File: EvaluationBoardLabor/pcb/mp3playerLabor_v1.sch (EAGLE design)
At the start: 25 parts, among them IC1 4050N, Q1 12MHz, X1 FPS009-3000, X2 1503_09

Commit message: update schematic
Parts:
- added LED1, LED2, LED3: (no value), led:LEDSML1206
- added R10, R11, R12: 390, rcl:R-EU_R1206
- added R2, R8, R9: 100k, rcl:R-EU_R1206
- added SV5: (no value), con-lstb:MA04-1
- R1, R3, R4, R5, R6, R7: device rcl:R-EU_M1206 -> rcl:R-EU_R1206
- X1: value FPS009-3000 -> SD-Card holder
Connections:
- removed net AREF: SV3.3
- removed net N$1: U$1.P$12, X1.5
- removed net N$15: U$1.P$1
- removed net N$17: R7.1, U$1.P$26
- removed net N$2: U$1.P$14, X1.7
- removed net N$3: U$1.P$13, X1.2
- new net CSCARD: IC1C.O, X1.1
- new net MOSI: IC1B.O, U$1.P$13, X1.2
- new net SCK: IC1A.O, U$1.P$12, X1.5
- new net XCS: IC1D.O, U$1.P$11
- new net XDCS: IC1E.O, U$1.P$4
- new net XRESET: IC1F.O, R7.1, U$1.P$26
- net +3V3: now also C5.1, IC1P.VDD, SV3.3
- net +5V: now also S1.S, S2.S, S3.S, SV5.2
- net GND: now also C5.2, R10.2, R11.2, R12.2, R2.2, R8.2, R9.2, SV5.1
- net N$4: now also LED1.C, R10.1; no longer U$1.P$11
- net N$5: now also LED2.C, R11.1; no longer X1.1
- net N$7: now also LED3.C, R12.1; no longer U$1.P$4
- net PB1: now also IC1C.I
- net PB2: now also IC1D.I
- net PB3: now also IC1B.I
- net PB4: now also U$1.P$14, X1.7
- net PB5: now also IC1A.I
- net PC0: now also IC1E.I
- net PC1: now also U$1.P$1
- net PC3: now also IC1F.I
- net PC4: now also SV5.4
- net PC5: now also SV5.3
- net PD2: now also R2.1, S1.P
- net PD3: now also R8.1, S2.P
- net PD4: now also R9.1, S3.P
- net PD5: now also LED1.A
- net PD6: now also LED2.A
- net PD7: now also LED3.A
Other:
- note added: "(DREQ)"
- note added: "(MISO)"
- note added: "(SCL)"
- note added: "(SDA)"
- note added: "ATmega328-XPlained"
- note added: "I2C Display"
- note added: "Level Shifter (5V->3,3V)"
- note added: "MP3-Decoder"
- note added: "PB0 = PB1 = CS Card PB2 = XCS (MP3-Decoder) PB3 = MOSI (SPI) PB4 = MISO (SPI) PB5 = SCK (SPI)"
- note added: "PC0 = XDCS (MP3-Decoder) PC1 = DREQ (MP3-Decoder) PC2 = PC3 = XRESET (MP3-Decoder) PC4 = SDA ( I2C Display ) PC5 = SCL ( I2C Display )"
- note added: "PD0 = RX PD1 = TX PD2 = S1 Taster PD3 = S2 Taster PD4 = S3 Taster PD5 = LED1 PD6 = LED2 PD7 = LED3"
- moved on the sheet: C5, IC1A, IC1B, IC1C, IC1D, IC1E, IC1F, IC1P, S1, S2, S3

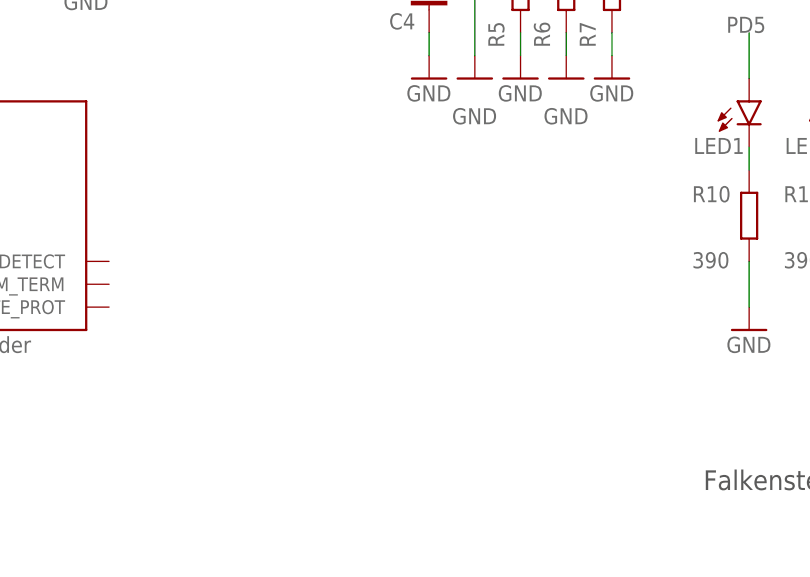
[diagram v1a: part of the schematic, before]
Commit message: DisplayTest added
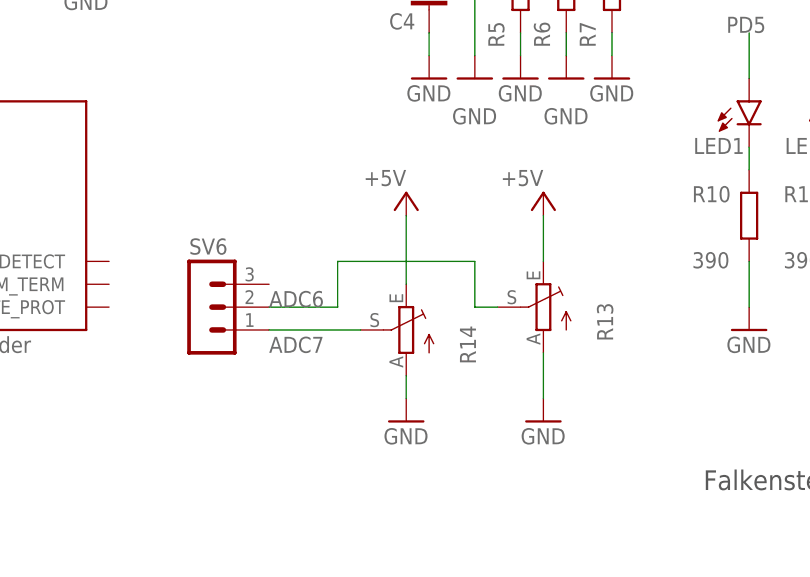
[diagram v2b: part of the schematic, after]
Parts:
- added R13, R14: (no value), pot:TRIM_EU-CA6V
- added SV6: (no value), con-lstb:MA03-1
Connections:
- new net ADC6: R13.S, SV6.2
- new net ADC7: R14.S, SV6.1
- net +5V: now also R13.E, R14.E
- net GND: now also R13.A, R14.A
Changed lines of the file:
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@@
 <part name="GND21" library="supply1" deviceset="GND" device=""/>
 <part name="GND22" library="supply1" deviceset="GND" device=""/>
+<part name="SV6" library="con-lstb" library_urn="urn:adsk.eagle:library:162" deviceset="MA03-1" device="" package3d_urn="urn:adsk.eagle:package:8339/1"/>
+<part name="R13" library="pot" library_urn="urn:adsk.eagle:library:331" deviceset="TRIM_EU-" device="CA6V" package3d_urn="urn:adsk.eagle:package:22691/1"/>
+<part name="R14" library="pot" library_urn="urn:adsk.eagle:library:331" deviceset="TRIM_EU-" device="CA6V" package3d_urn="urn:adsk.eagle:package:22691/1"/>
+<part name="GND15" library="supply1" deviceset="GND" device=""/>
+<part name="GND23" library="supply1" deviceset="GND" device=""/>
+<part name="P+6" library="supply1" library_urn="urn:adsk.eagle:library:371" deviceset="+5V" device=""/>
+<part name="P+7" library="supply1" library_urn="urn:adsk.eagle:library:371" deviceset="+5V" device=""/>
 </parts>
 <sheets>
@@
 <attribute name="VALUE" x="241.3" y="35.56" size="1.778" layer="96"/>
 </instance>
+<instance part="SV6" gate="G$1" x="162.56" y="40.64" smashed="yes">
+<attribute name="VALUE" x="161.29" y="33.02" size="1.778" layer="96"/>
+<attribute name="NAME" x="161.29" y="46.482" size="1.778" layer="95"/>
+</instance>
+<instance part="R13" gate="1" x="200.66" y="40.64" smashed="yes" rot="MR0">
+<attribute name="NAME" x="206.629" y="36.83" size="1.778" layer="95" rot="MR90"/>
+<attribute name="VALUE" x="204.47" y="36.83" size="1.778" layer="96" rot="MR90"/>
+</instance>
+<instance part="R14" gate="1" x="185.42" y="38.1" smashed="yes" rot="MR0">
+<attribute name="NAME" x="191.389" y="34.29" size="1.778" layer="95" rot="MR90"/>
+<attribute name="VALUE" x="189.23" y="34.29" size="1.778" layer="96" rot="MR90"/>
+</instance>
+<instance part="GND15" gate="1" x="200.66" y="27.94" smashed="yes">
+<attribute name="VALUE" x="198.12" y="25.4" size="1.778" layer="96"/>
+</instance>
+<instance part="GND23" gate="1" x="185.42" y="27.94" smashed="yes">
+<attribute name="VALUE" x="182.88" y="25.4" size="1.778" layer="96"/>
+</instance>
+<instance part="P+6" gate="1" x="200.66" y="53.34" smashed="yes">
+<attribute name="VALUE" x="200.66" y="55.88" size="1.778" layer="96" rot="R180"/>
+</instance>
+<instance part="P+7" gate="1" x="185.42" y="53.34" smashed="yes">
+<attribute name="VALUE" x="185.42" y="55.88" size="1.778" layer="96" rot="R180"/>
+</instance>
 </instances>
 <busses>
@@
 <wire x1="243.84" y1="45.72" x2="243.84" y2="40.64" width="0.1524" layer="91"/>
 </segment>
+<segment>
+<pinref part="R14" gate="1" pin="A"/>
+<pinref part="GND23" gate="1" pin="GND"/>
+<wire x1="185.42" y1="33.02" x2="185.42" y2="30.48" width="0.1524" layer="91"/>
+</segment>
+<segment>
+<pinref part="R13" gate="1" pin="A"/>
+<pinref part="GND15" gate="1" pin="GND"/>
+<wire x1="200.66" y1="35.56" x2="200.66" y2="30.48" width="0.1524" layer="91"/>
+</segment>
 </net>
 <net name="N$10" class="0">
@@
 <wire x1="251.46" y1="167.64" x2="251.46" y2="162.56" width="0.1524" layer="91"/>
 </segment>
+<segment>
+<pinref part="R13" gate="1" pin="E"/>
+<pinref part="P+6" gate="1" pin="+5V"/>
+<wire x1="200.66" y1="45.72" x2="200.66" y2="50.8" width="0.1524" layer="91"/>
+</segment>
+<segment>
+<pinref part="R14" gate="1" pin="E"/>
+<pinref part="P+7" gate="1" pin="+5V"/>
+<wire x1="185.42" y1="43.18" x2="185.42" y2="50.8" width="0.1524" layer="91"/>
+</segment>
 </net>
 <net name="VIN" class="0">
@@
 </segment>
 </net>
+<net name="ADC7" class="0">
+<segment>
+<pinref part="SV6" gate="G$1" pin="1"/>
+<label x="170.18" y="35.56" size="1.778" layer="95"/>
+<pinref part="R14" gate="1" pin="S"/>
+<wire x1="180.34" y1="38.1" x2="170.18" y2="38.1" width="0.1524" layer="91"/>
+</segment>
+</net>
+<net name="ADC6" class="0">
+<segment>
+<pinref part="SV6" gate="G$1" pin="2"/>
+<label x="170.18" y="40.64" size="1.778" layer="95"/>
+<pinref part="R13" gate="1" pin="S"/>
+<wire x1="195.58" y1="40.64" x2="193.04" y2="40.64" width="0.1524" layer="91"/>
+<wire x1="193.04" y1="40.64" x2="193.04" y2="45.72" width="0.1524" layer="91"/>
+<wire x1="193.04" y1="45.72" x2="177.8" y2="45.72" width="0.1524" layer="91"/>
+<wire x1="177.8" y1="45.72" x2="177.8" y2="40.64" width="0.1524" layer="91"/>
+<wire x1="177.8" y1="40.64" x2="170.18" y2="40.64" width="0.1524" layer="91"/>
+</segment>
+</net>

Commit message: update pcb
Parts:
- added R15, R16: 100k, rcl:R-EU_R1206
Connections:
- net +5V: now also R15.1, R16.1
- net PC4: now also R16.2
- net PC5: now also R15.2
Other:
- moved on the sheet: SV5
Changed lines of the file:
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@@
 <part name="P+6" library="supply1" library_urn="urn:adsk.eagle:library:371" deviceset="+5V" device=""/>
 <part name="P+7" library="supply1" library_urn="urn:adsk.eagle:library:371" deviceset="+5V" device=""/>
+<part name="R15" library="rcl" library_urn="urn:adsk.eagle:library:334" deviceset="R-EU_" device="R1206" package3d_urn="urn:adsk.eagle:package:23540/2" value="100k"/>
+<part name="R16" library="rcl" library_urn="urn:adsk.eagle:library:334" deviceset="R-EU_" device="R1206" package3d_urn="urn:adsk.eagle:package:23540/2" value="100k"/>
 </parts>
 <sheets>
@@
 <text x="162.56" y="76.2" size="1.778" layer="96">MP3-Decoder</text>
 <text x="96.52" y="121.92" size="1.778" layer="97">(DREQ)</text>
-<text x="96.52" y="152.4" size="1.778" layer="97">(SCL)</text>
-<text x="96.52" y="149.86" size="1.778" layer="96">(SDA)</text>
+<text x="91.44" y="147.32" size="1.778" layer="97">(SCL)</text>
+<text x="91.44" y="144.78" size="1.778" layer="96">(SDA)</text>
 <wire x1="88.9" y1="170.18" x2="134.62" y2="170.18" width="0.1524" layer="97"/>
 <wire x1="134.62" y1="170.18" x2="134.62" y2="139.7" width="0.1524" layer="97"/>
@@
 <attribute name="VALUE" x="71.12" y="165.1" size="1.778" layer="96" rot="R180"/>
 </instance>
-<instance part="SV5" gate="1" x="127" y="152.4" smashed="yes" rot="R180">
-<attribute name="VALUE" x="128.27" y="162.56" size="1.778" layer="96" rot="R180"/>
-<attribute name="NAME" x="128.27" y="146.558" size="1.778" layer="95" rot="R180"/>
-</instance>
-<instance part="GND16" gate="1" x="114.3" y="157.48" smashed="yes" rot="R270">
-<attribute name="VALUE" x="111.76" y="160.02" size="1.778" layer="96"/>
-</instance>
-<instance part="P+2" gate="1" x="109.22" y="165.1" smashed="yes">
-<attribute name="VALUE" x="109.22" y="167.64" size="1.778" layer="96" rot="R180"/>
+<instance part="SV5" gate="1" x="132.08" y="147.32" smashed="yes" rot="R180">
+<attribute name="VALUE" x="133.35" y="157.48" size="1.778" layer="96" rot="R180"/>
+<attribute name="NAME" x="133.35" y="141.478" size="1.778" layer="95" rot="R180"/>
+</instance>
+<instance part="GND16" gate="1" x="114.3" y="152.4" smashed="yes" rot="R270">
+<attribute name="VALUE" x="119.38" y="152.4" size="1.778" layer="96"/>
+</instance>
+<instance part="P+2" gate="1" x="109.22" y="167.64" smashed="yes">
+<attribute name="VALUE" x="116.84" y="167.64" size="1.778" layer="96" rot="R180"/>
 </instance>
 <instance part="R2" gate="G$1" x="226.06" y="144.78" smashed="yes" rot="R270">
@@
 <instance part="P+7" gate="1" x="185.42" y="53.34" smashed="yes">
 <attribute name="VALUE" x="185.42" y="55.88" size="1.778" layer="96" rot="R180"/>
+</instance>
+<instance part="R15" gate="G$1" x="101.6" y="154.94" smashed="yes" rot="R270">
+<attribute name="NAME" x="95.25" y="156.4386" size="1.778" layer="95"/>
+<attribute name="VALUE" x="95.25" y="151.638" size="1.778" layer="96"/>
+</instance>
+<instance part="R16" gate="G$1" x="106.68" y="154.94" smashed="yes" rot="R270">
+<attribute name="NAME" x="110.49" y="158.9786" size="1.778" layer="95"/>
+<attribute name="VALUE" x="110.49" y="156.718" size="1.778" layer="96"/>
 </instance>
 </instances>
@@
 <pinref part="SV5" gate="1" pin="1"/>
 <pinref part="GND16" gate="1" pin="GND"/>
-<wire x1="119.38" y1="157.48" x2="116.84" y2="157.48" width="0.1524" layer="91"/>
+<wire x1="124.46" y1="152.4" x2="116.84" y2="152.4" width="0.1524" layer="91"/>
 </segment>
 <segment>
@@
 <pinref part="SV5" gate="1" pin="2"/>
 <pinref part="P+2" gate="1" pin="+5V"/>
-<wire x1="119.38" y1="154.94" x2="109.22" y2="154.94" width="0.1524" layer="91"/>
-<wire x1="109.22" y1="154.94" x2="109.22" y2="162.56" width="0.1524" layer="91"/>
+<wire x1="124.46" y1="149.86" x2="109.22" y2="149.86" width="0.1524" layer="91"/>
+<wire x1="109.22" y1="149.86" x2="109.22" y2="160.02" width="0.1524" layer="91"/>
+<pinref part="R16" gate="G$1" pin="1"/>
+<wire x1="109.22" y1="160.02" x2="109.22" y2="162.56" width="0.1524" layer="91"/>
+<wire x1="109.22" y1="162.56" x2="109.22" y2="165.1" width="0.1524" layer="91"/>
+<wire x1="106.68" y1="160.02" x2="109.22" y2="160.02" width="0.1524" layer="91"/>
+<junction x="109.22" y="160.02"/>
+<pinref part="R15" gate="G$1" pin="1"/>
+<wire x1="101.6" y1="160.02" x2="101.6" y2="162.56" width="0.1524" layer="91"/>
+<wire x1="101.6" y1="162.56" x2="109.22" y2="162.56" width="0.1524" layer="91"/>
+<junction x="109.22" y="162.56"/>
 </segment>
 <segment>
@@
 <segment>
 <pinref part="SV5" gate="1" pin="4"/>
-<wire x1="119.38" y1="149.86" x2="109.22" y2="149.86" width="0.1524" layer="91"/>
-<label x="104.14" y="149.86" size="1.778" layer="95"/>
+<wire x1="124.46" y1="144.78" x2="106.68" y2="144.78" width="0.1524" layer="91"/>
+<label x="99.06" y="144.78" size="1.778" layer="95"/>
+<pinref part="R16" gate="G$1" pin="2"/>
+<wire x1="106.68" y1="144.78" x2="99.06" y2="144.78" width="0.1524" layer="91"/>
+<wire x1="106.68" y1="149.86" x2="106.68" y2="144.78" width="0.1524" layer="91"/>
+<junction x="106.68" y="144.78"/>
 </segment>
 </net>
@@
 <segment>
 <pinref part="SV5" gate="1" pin="3"/>
-<wire x1="119.38" y1="152.4" x2="109.22" y2="152.4" width="0.1524" layer="91"/>
-<label x="104.14" y="152.4" size="1.778" layer="95"/>
-</segment>
-</net>
+<wire x1="124.46" y1="147.32" x2="101.6" y2="147.32" width="0.1524" layer="91"/>
+<label x="99.06" y="147.32" size="1.778" layer="95"/>
+<pinref part="R15" gate="G$1" pin="2"/>
+<wire x1="101.6" y1="147.32" x2="99.06" y2="147.32" width="0.1524" layer="91"/>
+<wire x1="101.6" y1="149.86" x2="101.6" y2="147.32" width="0.1524" layer="91"/>
+<junction x="101.6" y="147.32"/>
+</segment>
+</net>

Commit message: pcb finished, 1st version
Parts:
- R13, R14: value (none) -> 10k
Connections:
- net PC4: no longer SV3.2
- net PC5: no longer SV3.1
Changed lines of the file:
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@@
 <part name="GND22" library="supply1" deviceset="GND" device=""/>
 <part name="SV6" library="con-lstb" library_urn="urn:adsk.eagle:library:162" deviceset="MA03-1" device="" package3d_urn="urn:adsk.eagle:package:8339/1"/>
-<part name="R13" library="pot" library_urn="urn:adsk.eagle:library:331" deviceset="TRIM_EU-" device="CA6V" package3d_urn="urn:adsk.eagle:package:22691/1"/>
-<part name="R14" library="pot" library_urn="urn:adsk.eagle:library:331" deviceset="TRIM_EU-" device="CA6V" package3d_urn="urn:adsk.eagle:package:22691/1"/>
+<part name="R13" library="pot" library_urn="urn:adsk.eagle:library:331" deviceset="TRIM_EU-" device="CA6V" package3d_urn="urn:adsk.eagle:package:22691/1" value="10k"/>
+<part name="R14" library="pot" library_urn="urn:adsk.eagle:library:331" deviceset="TRIM_EU-" device="CA6V" package3d_urn="urn:adsk.eagle:package:22691/1" value="10k"/>
 <part name="GND15" library="supply1" deviceset="GND" device=""/>
 <part name="GND23" library="supply1" deviceset="GND" device=""/>
@@
 </segment>
 <segment>
-<pinref part="SV3" gate="G$1" pin="2"/>
-<wire x1="55.88" y1="157.48" x2="58.42" y2="157.48" width="0.1524" layer="91"/>
-<label x="58.42" y="157.48" size="1.778" layer="95"/>
-</segment>
-<segment>
 <pinref part="SV5" gate="1" pin="4"/>
 <wire x1="124.46" y1="144.78" x2="106.68" y2="144.78" width="0.1524" layer="91"/>
@@
 </segment>
 <segment>
-<pinref part="SV3" gate="G$1" pin="1"/>
-<wire x1="55.88" y1="160.02" x2="58.42" y2="160.02" width="0.1524" layer="91"/>
-<label x="58.42" y="160.02" size="1.778" layer="95"/>
-</segment>
-<segment>

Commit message: pcb finished and order sent to jlcpcb
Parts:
- Q1: value 12MHz -> 12,288 MHz
- X1: value SD-Card holder -> SD-Card
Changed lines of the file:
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@@
 <part name="U$1" library="vs10xx" deviceset="VS1011" device=""/>
 <part name="FRAME1" library="frames" deviceset="A4L-LOC" device=""/>
-<part name="X1" library="con-yamaichi" deviceset="FPS009-300*" device="" technology="0" value="SD-Card holder"/>
-<part name="Q1" library="crystal" deviceset="CRYSTAL" device="HC49UP" value="12MHz"/>
+<part name="X1" library="con-yamaichi" deviceset="FPS009-300*" device="" technology="0" value="SD-Card"/>
+<part name="Q1" library="crystal" deviceset="CRYSTAL" device="HC49UP" value="12,288 MHz"/>
 <part name="GND1" library="supply1" deviceset="GND" device=""/>
 <part name="GND3" library="supply1" deviceset="GND" device=""/>
